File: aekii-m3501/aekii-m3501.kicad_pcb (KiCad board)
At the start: 2 copper layers, 21 x 21 mm, 2 parts, among them J2 Conn_01x04

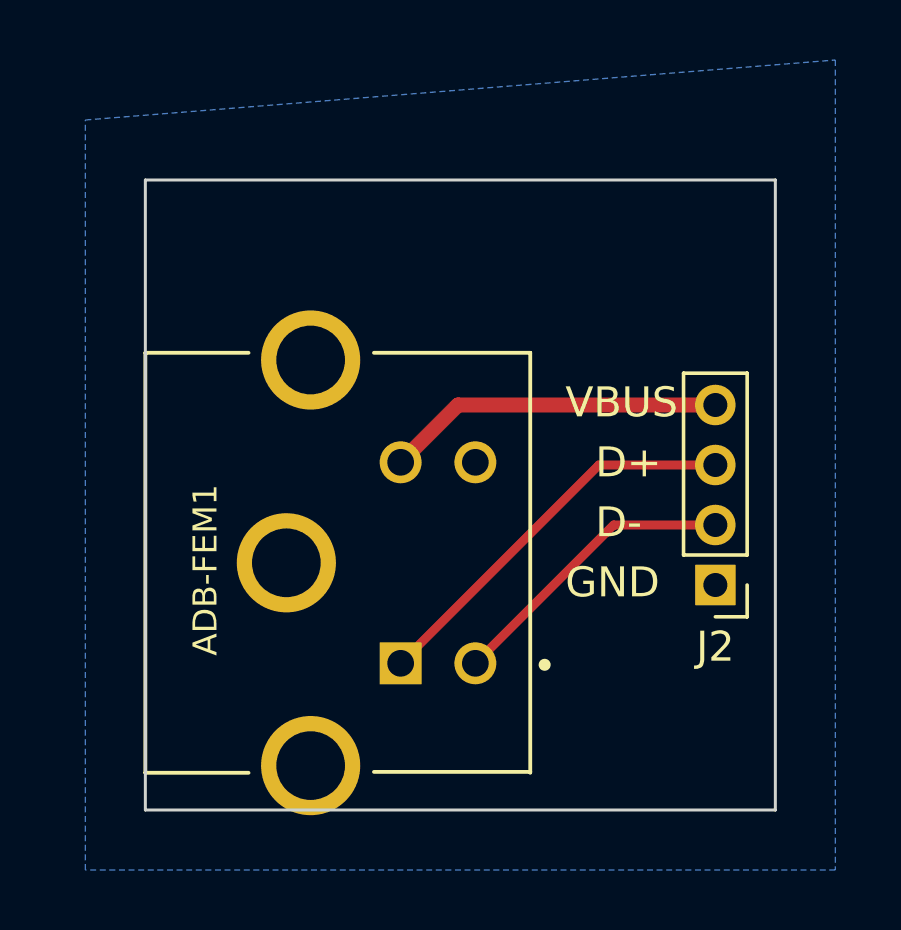
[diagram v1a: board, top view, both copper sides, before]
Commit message: switched D+/D- on USB PCB, isolated shield from ground
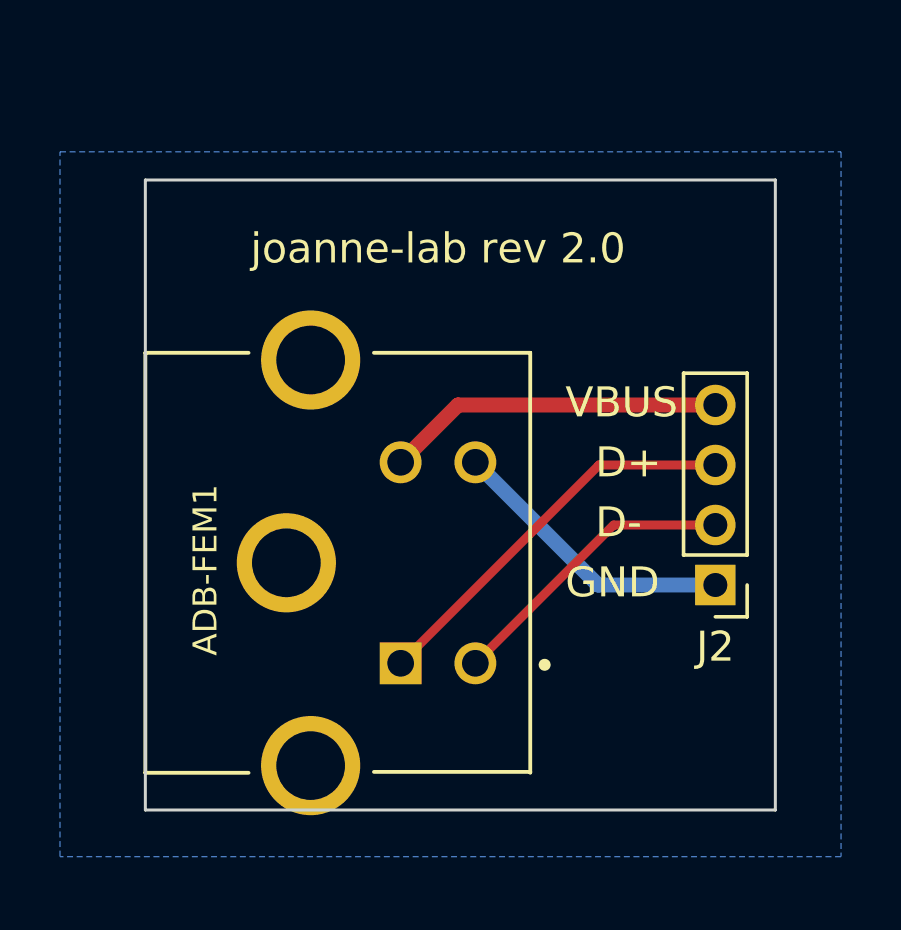
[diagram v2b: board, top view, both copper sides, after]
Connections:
- ADB-FEM1 pad 5: GND -> unconnected-(ADB-FEM1-SH-Pad5)
- ADB-FEM1 pad 6: GND -> unconnected-(ADB-FEM1-SH-Pad5)
- ADB-FEM1 pad 7: GND -> unconnected-(ADB-FEM1-SH-Pad5)
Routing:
- net GND: track 0.00 -> 9.69 mm
- added copper zone on B.Cu, net (none)
- removed copper zone on B.Cu, net GND
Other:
- board text added: "joanne-lab rev 2.0"
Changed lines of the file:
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@@
       (outputformat 1)
       (mirror false)
-      (drillshape 1)
+      (drillshape 0)
       (scaleselection 1)
-      (outputdirectory "")
+      (outputdirectory "../fabrication/aekii-m3501/")
     )
   )
@@
   (net 3 "VBUS")
   (net 4 "GND")
+  (net 5 "unconnected-(ADB-FEM1-SH-Pad5)")
   (footprint "ADB:TE_5749181-1" (layer "F.Cu")
     (at 108.51 112.76 90)
@@
       (net 4 "GND") (pinfunction "4") (pintype "passive") (solder_mask_margin 0.102))
     (pad "5" thru_hole circle (at 0 -3.81 90) (size 3.306 3.306) (drill 2.29) (layers "*.Cu" "*.Mask")
-      (net 4 "GND") (pinfunction "SH") (pintype "passive") (solder_mask_margin 0.102))
+      (net 5 "unconnected-(ADB-FEM1-SH-Pad5)") (pinfunction "SH") (pintype "passive+no_connect") (solder_mask_margin 0.102))
     (pad "6" thru_hole circle (at 6.76 -3 90) (size 3.306 3.306) (drill 2.29) (layers "*.Cu" "*.Mask")
-      (net 4 "GND") (pinfunction "SH") (pintype "passive") (solder_mask_margin 0.102))
+      (net 5 "unconnected-(ADB-FEM1-SH-Pad5)") (pinfunction "SH") (pintype "passive+no_connect") (solder_mask_margin 0.102))
     (pad "7" thru_hole circle (at -6.76 -3 90) (size 3.306 3.306) (drill 2.29) (layers "*.Cu" "*.Mask")
-      (net 4 "GND") (pinfunction "SH") (pintype "passive") (solder_mask_margin 0.102))
+      (net 5 "unconnected-(ADB-FEM1-SH-Pad5)") (pinfunction "SH") (pintype "passive+no_connect") (solder_mask_margin 0.102))
   )
   (footprint "Connector_PinHeader_2.00mm:PinHeader_1x04_P2.00mm_Vertical" (layer "F.Cu")
@@
     (effects (font (size 1 1) (thickness 0.15)) (justify left bottom))
   )
+  (gr_text "joanne-lab rev 2.0" (at 103.505 102.87) (layer "F.SilkS")
+    (effects (font (size 1 1) (thickness 0.15)) (justify left bottom))
+  )
   (gr_text "D-\n" (at 115 112) (layer "F.SilkS")
     (effects (font (size 1 1) (thickness 0.15)) (justify left bottom))
@@
   (segment (start 110.42 107.5) (end 108.51 109.41) (width 0.5) (layer "F.Cu") (net 3))
   (segment (start 119 107.5) (end 110.42 107.5) (width 0.5) (layer "F.Cu") (net 3))
-  (zone (net 4) (net_name "GND") (layer "B.Cu") (hatch edge 0.5)
+  (segment (start 119 113.5) (end 115.09 113.5) (width 0.5) (layer "B.Cu") (net 4))
+  (segment (start 115.09 113.5) (end 111 109.41) (width 0.5) (layer "B.Cu") (net 4))
+  (zone (net 0) (net_name "") (layer "B.Cu") (hatch edge 0.5)
     (connect_pads (clearance 0.5))
     (min_thickness 0.25) (filled_areas_thickness no)
-    (fill yes (thermal_gap 0.5) (thermal_bridge_width 0.5))
+    (fill yes (thermal_gap 0.5) (thermal_bridge_width 0.5) (island_removal_mode 1) (island_area_min 10))
     (polygon
       (pts
-        (xy 123 96)
-        (xy 123 123)
-        (xy 98 123)
-        (xy 98 98)
+        (xy 123.19 99.06)
+        (xy 123.19 122.555)
+        (xy 97.155 122.555)
+        (xy 97.155 99.06)
       )
     )
